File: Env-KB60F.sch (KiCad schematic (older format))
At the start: 141 parts, among them SW1 EVQ-P7A01P, U1 Pico

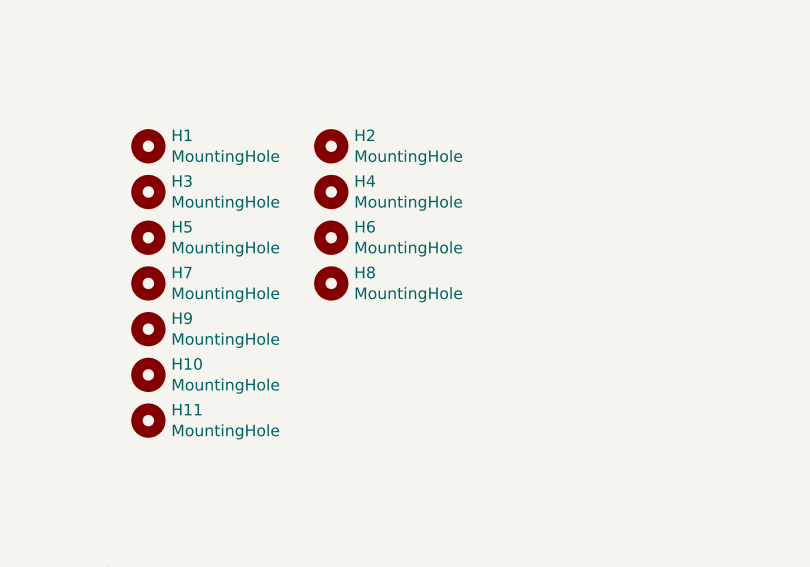
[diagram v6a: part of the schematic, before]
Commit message: Designed New Plate, adjusted mount holes and fixed trace issues.
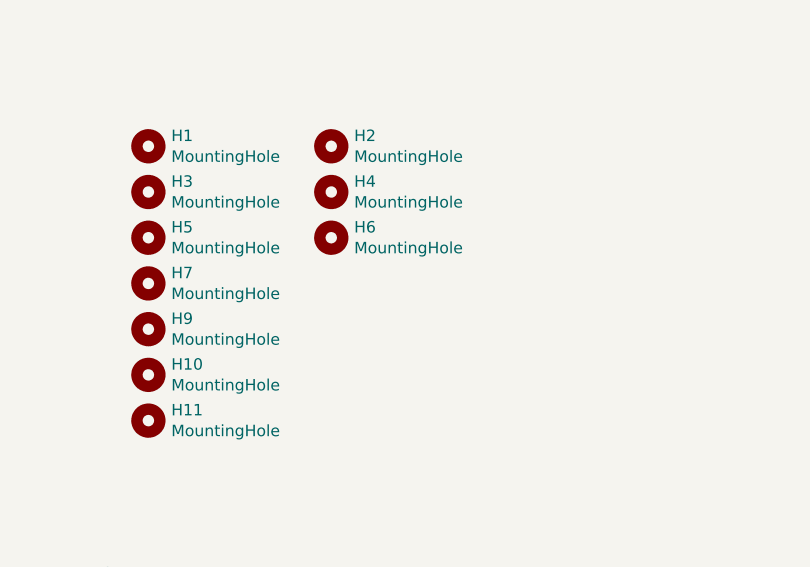
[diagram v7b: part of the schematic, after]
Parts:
- removed H8: MountingHole, MountingHole:MountingHole_2.1mm, symbol Mechanical:MountingHole
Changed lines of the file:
@@
-$EndComp
-$Comp
-L Mechanical:MountingHole H8
-U 1 1 60938A01
-P 6400 6950
-F 0 "H8" H 6500 6996 50  0000 L CNN
-F 1 "MountingHole" H 6500 6905 50  0000 L CNN
-F 2 "MountingHole:MountingHole_2.1mm" H 6400 6950 50  0001 C CNN
-F 3 "~" H 6400 6950 50  0001 C CNN
-	1    6400 6950
-	1    0    0    -1
 $EndComp
 $Comp

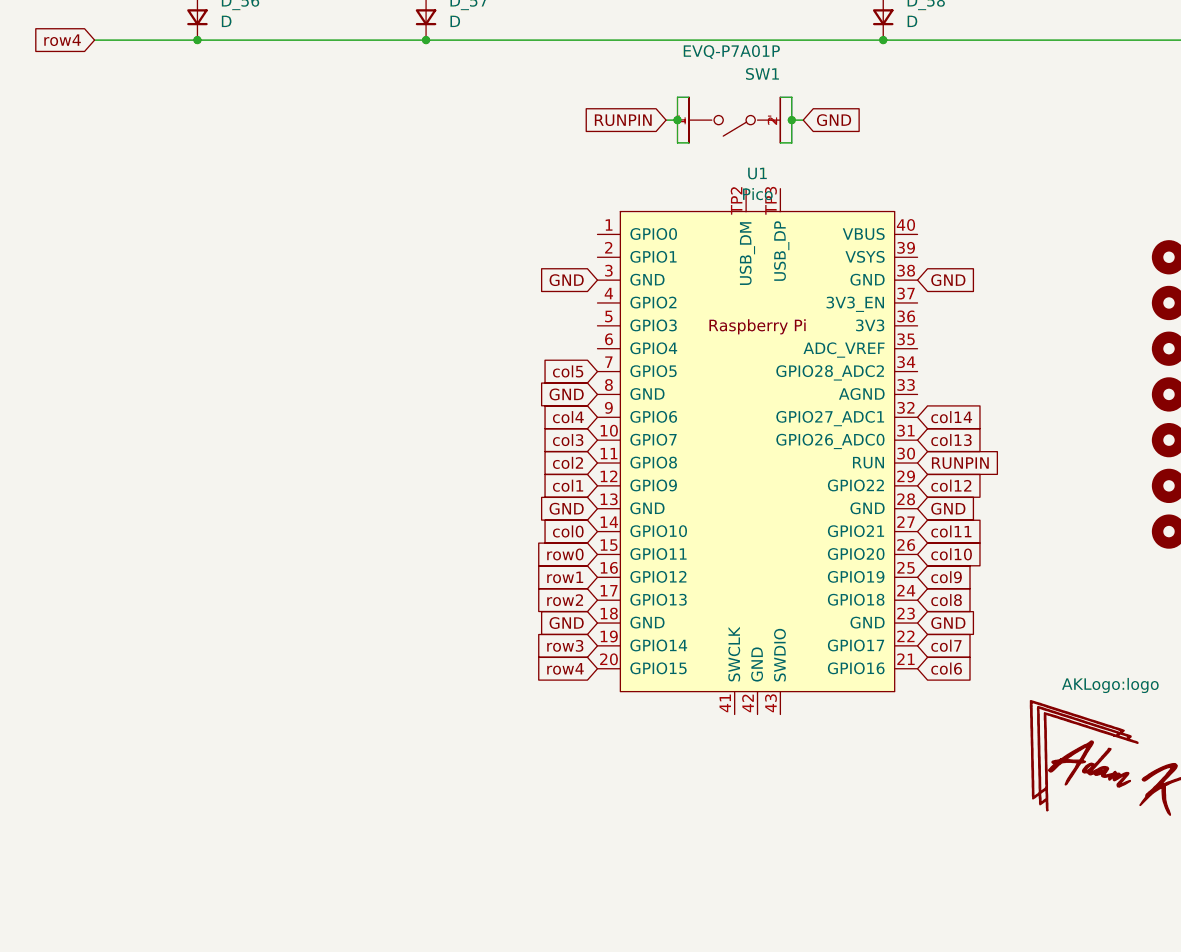
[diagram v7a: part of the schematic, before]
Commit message: Added a optional top USB port based on feedback
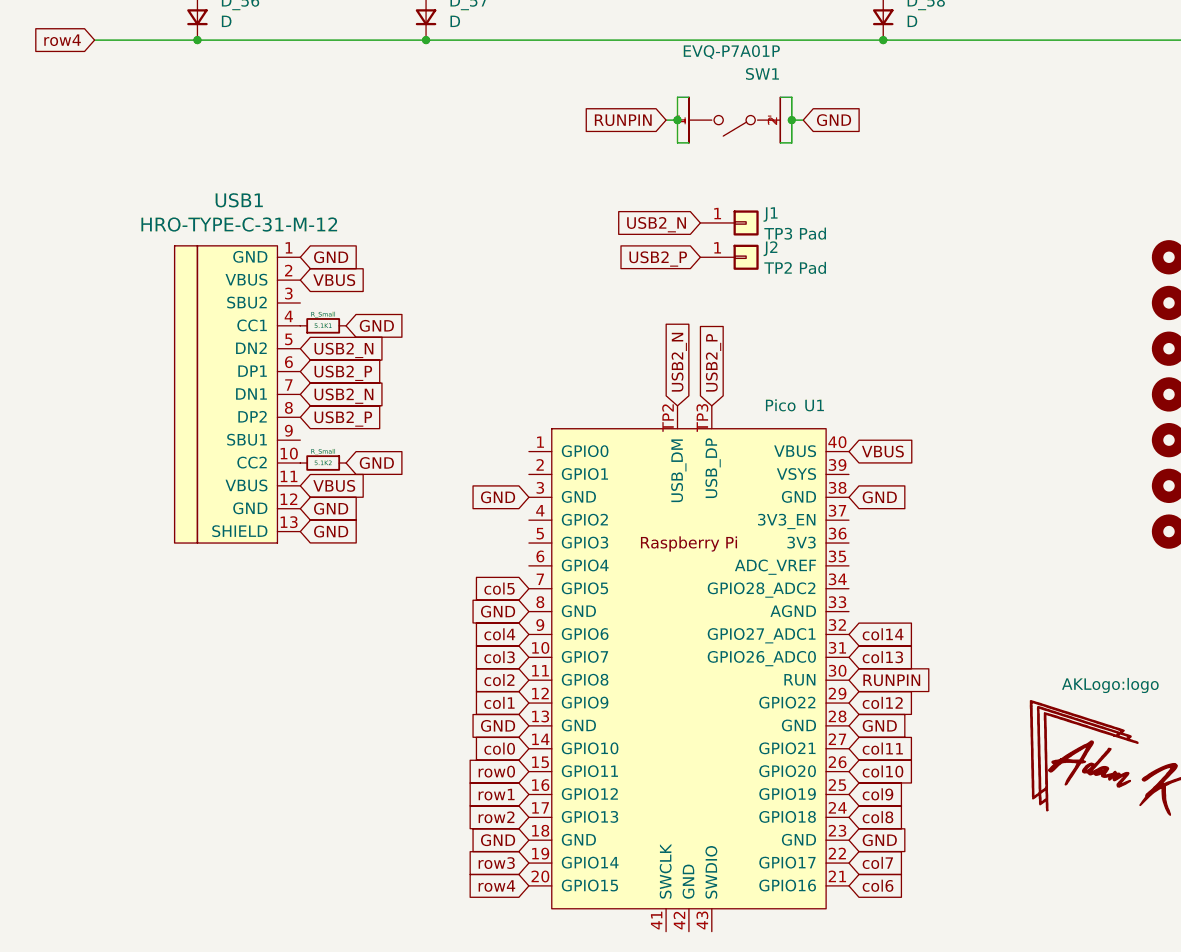
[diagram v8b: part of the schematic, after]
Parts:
- added 5.1K1, 5.1K2: R_Small, Resistor_SMD:R_0201_0603Metric, symbol Device:R_Small
- added J1: TP3 Pad, TestPoint:TestPoint_Pad_1.0x1.0mm, symbol Connector_Generic:Conn_01x01
- added J2: TP2 Pad, TestPoint:TestPoint_Pad_1.0x1.0mm, symbol Connector_Generic:Conn_01x01
- added USB1: HRO-TYPE-C-31-M-12, HRO-TYPE-C31-M-12:HRO-TYPE-C-31-M-12, symbol Type-C:HRO-TYPE-C-31-M-12
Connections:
- net GND: now also 5.1K1.2, 5.1K2.1, USB1.1 (GND), USB1.12 (GND), USB1.13 (SHIELD)
- net VBUS: now reaches U1.40 (VBUS)
- net VBUS: now also USB1.11 (VBUS), USB1.2 (VBUS)
- net USB2_N: now reaches U1.TP2 (USB_DM)
- net USB2_N: now also J1.1 (Pin_1), USB1.5 (DN2), USB1.7 (DN1)
- net USB2_P: now reaches U1.TP3 (USB_DP)
- net USB2_P: now also J2.1 (Pin_1), USB1.6 (DP1), USB1.8 (DP2)
- new net: 5.1K2.2, USB1.10 (CC2)
- new net: 5.1K1.1, USB1.4 (CC1)
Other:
- moved on the sheet: U1
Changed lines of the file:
@@
 L MCU_RaspberryPi_and_Boards:Pico U1
 U 1 1 6095EAE7
-P 3800 7200
-F 0 "U1" H 3800 8415 50  0000 C CNN
-F 1 "Pico" H 3800 8324 50  0000 C CNN
-F 2 "MCU_RaspberryPi_and_Boards:RPi_Pico_SMD_TH" V 3800 7200 50  0001 C CNN
-F 3 "" H 3800 7200 50  0001 C CNN
-	1    3800 7200
-	1    0    0    -1
-$EndComp
-Text GLabel 3100 6950 0    50   Input ~ 0
-GND
-Text GLabel 3100 7450 0    50   Input ~ 0
-GND
-Text GLabel 3100 7950 0    50   Input ~ 0
-GND
-Text GLabel 3100 6450 0    50   Input ~ 0
-GND
-Text GLabel 4500 6450 2    50   Input ~ 0
-GND
-Text GLabel 4500 7450 2    50   Input ~ 0
-GND
-Text GLabel 4500 7950 2    50   Input ~ 0
-GND
-Text GLabel 3100 7650 0    50   Input ~ 0
+P 3500 8150
+F 0 "U1" H 4050 9300 50  0000 C CNN
+F 1 "Pico" H 3900 9300 50  0000 C CNN
+F 2 "MCU_RaspberryPi_and_Boards:RPi_Pico_SMD_TH" V 3500 8150 50  0001 C CNN
+F 3 "" H 3500 8150 50  0001 C CNN
+	1    3500 8150
+	1    0    0    -1
+$EndComp
+Text GLabel 2800 7900 0    50   Input ~ 0
+GND
+Text GLabel 2800 8400 0    50   Input ~ 0
+GND
+Text GLabel 2800 8900 0    50   Input ~ 0
+GND
+Text GLabel 2800 7400 0    50   Input ~ 0
+GND
+Text GLabel 4200 7400 2    50   Input ~ 0
+GND
+Text GLabel 4200 8400 2    50   Input ~ 0
+GND
+Text GLabel 4200 8900 2    50   Input ~ 0
+GND
+Text GLabel 2800 8600 0    50   Input ~ 0
 row0
-Text GLabel 3100 7750 0    50   Input ~ 0
+Text GLabel 2800 8700 0    50   Input ~ 0
 row1
-Text GLabel 3100 7850 0    50   Input ~ 0
+Text GLabel 2800 8800 0    50   Input ~ 0
 row2
-Text GLabel 3100 8050 0    50   Input ~ 0
+Text GLabel 2800 9000 0    50   Input ~ 0
 row3
-Text GLabel 3100 8150 0    50   Input ~ 0
+Text GLabel 2800 9100 0    50   Input ~ 0
 row4
-Text GLabel 3100 7550 0    50   Input ~ 0
+Text GLabel 2800 8500 0    50   Input ~ 0
 col0
-Text GLabel 3100 7350 0    50   Input ~ 0
+Text GLabel 2800 8300 0    50   Input ~ 0
 col1
-Text GLabel 3100 7250 0    50   Input ~ 0
+Text GLabel 2800 8200 0    50   Input ~ 0
 col2
-Text GLabel 3100 7150 0    50   Input ~ 0
+Text GLabel 2800 8100 0    50   Input ~ 0
 col3
-Text GLabel 3100 7050 0    50   Input ~ 0
+Text GLabel 2800 8000 0    50   Input ~ 0
 col4
-Text GLabel 3100 6850 0    50   Input ~ 0
+Text GLabel 2800 7800 0    50   Input ~ 0
 col5
-Text GLabel 4500 8150 2    50   Input ~ 0
+Text GLabel 4200 9100 2    50   Input ~ 0
 col6
-Text GLabel 4500 8050 2    50   Input ~ 0
+Text GLabel 4200 9000 2    50   Input ~ 0
 col7
-Text GLabel 4500 7850 2    50   Input ~ 0
+Text GLabel 4200 8800 2    50   Input ~ 0
 col8
-Text GLabel 4500 7750 2    50   Input ~ 0
+Text GLabel 4200 8700 2    50   Input ~ 0
 col9
-Text GLabel 4500 7650 2    50   Input ~ 0
+Text GLabel 4200 8600 2    50   Input ~ 0
 col10
-Text GLabel 4500 7550 2    50   Input ~ 0
+Text GLabel 4200 8500 2    50   Input ~ 0
 col11
-Text GLabel 4500 7350 2    50   Input ~ 0
+Text GLabel 4200 8300 2    50   Input ~ 0
 col12
-Text GLabel 4500 7150 2    50   Input ~ 0
+Text GLabel 4200 8100 2    50   Input ~ 0
 col13
-Text GLabel 4500 7050 2    50   Input ~ 0
+Text GLabel 4200 8000 2    50   Input ~ 0
 col14
 $Comp
@@
 	1    0    0    -1
 $EndComp
-Text GLabel 4500 7250 2    50   Input ~ 0
+Text GLabel 4200 8200 2    50   Input ~ 0
 RUNPIN
 Text GLabel 3400 5750 0    50   Input ~ 0
@@
 Text Notes 1200 3700 0    50   ~ 0
 ANSI Left Shift
+$Comp
+L Type-C:HRO-TYPE-C-31-M-12 USB1
+U 1 1 60A58FC0
+P 1700 6900
+F 0 "USB1" H 1533 7697 60  0000 C CNN
+F 1 "HRO-TYPE-C-31-M-12" H 1533 7591 60  0000 C CNN
+F 2 "HRO-TYPE-C31-M-12:HRO-TYPE-C-31-M-12" H 1700 6900 60  0001 C CNN
+F 3 "" H 1700 6900 60  0001 C CNN
+	1    1700 6900
+	1    0    0    -1
+$EndComp
+Text GLabel 3600 7000 1    50   Input ~ 0
+USB2_P
+Text GLabel 3450 7000 1    50   Input ~ 0
+USB2_N
+Text GLabel 1800 6750 2    50   Input ~ 0
+USB2_N
+Text GLabel 1800 6950 2    50   Input ~ 0
+USB2_N
+Text GLabel 1800 6850 2    50   Input ~ 0
+USB2_P
+Text GLabel 1800 7050 2    50   Input ~ 0
+USB2_P
+$Comp
+L Device:R_Small 5.1K2
+U 1 1 60AAC80F
+P 1900 7250
+F 0 "5.1K2" V 1900 7250 20  0000 C CNN
+F 1 "R_Small" V 1850 7250 20  0000 C CNN
+F 2 "Resistor_SMD:R_0201_0603Metric" H 1900 7250 50  0001 C CNN
+F 3 "~" H 1900 7250 50  0001 C CNN
+	1    1900 7250
+	0    1    1    0
+$EndComp
+$Comp
+L Device:R_Small 5.1K1
+U 1 1 60AAF05F
+P 1900 6650
+F 0 "5.1K1" V 1900 6650 20  0000 C CNN
+F 1 "R_Small" V 1950 6650 20  0000 C CNN
+F 2 "Resistor_SMD:R_0201_0603Metric" H 1900 6650 50  0001 C CNN
+F 3 "~" H 1900 6650 50  0001 C CNN
+	1    1900 6650
+	0    -1   -1   0
+$EndComp
+Text GLabel 1800 7450 2    50   Input ~ 0
+GND
+Text GLabel 1800 6350 2    50   Input ~ 0
+GND
+Text GLabel 2000 7250 2    50   Input ~ 0
+GND
+Text GLabel 2000 6650 2    50   Input ~ 0
+GND
+$Comp
+L Connector_Generic:Conn_01x01 J1
+U 1 1 60B4329C
+P 3750 6200
+F 0 "J1" H 3830 6242 50  0000 L CNN
+F 1 "TP3 Pad" H 3830 6151 50  0000 L CNN
+F 2 "TestPoint:TestPoint_Pad_1.0x1.0mm" H 3750 6200 50  0001 C CNN
+F 3 "~" H 3750 6200 50  0001 C CNN
+	1    3750 6200
+	1    0    0    -1
+$EndComp
+$Comp
+L Connector_Generic:Conn_01x01 J2
+U 1 1 60B44B24
+P 3750 6350
+F 0 "J2" H 3830 6392 50  0000 L CNN
+F 1 "TP2 Pad" H 3830 6301 50  0000 L CNN
+F 2 "TestPoint:TestPoint_Pad_1.0x1.0mm" H 3750 6350 50  0001 C CNN
+F 3 "~" H 3750 6350 50  0001 C CNN
+	1    3750 6350
+	1    0    0    -1
+$EndComp
+Text GLabel 3550 6200 0    50   Input ~ 0
+USB2_N
+Text GLabel 3550 6350 0    50   Input ~ 0
+USB2_P
+Text GLabel 1800 7550 2    50   Input ~ 0
+GND
+Text GLabel 1800 7350 2    50   Input ~ 0
+VBUS
+Text GLabel 1800 6450 2    50   Input ~ 0
+VBUS
+Text GLabel 4200 7200 2    50   Input ~ 0
+VBUS
 $EndSCHEMATC
